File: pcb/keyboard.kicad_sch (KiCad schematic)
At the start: 22 parts, among them J1 Conn_ARM_JTAG_SWD_10, SW1 SW_PUSH, U1 nRF52840-QFXX, X1 32MHz

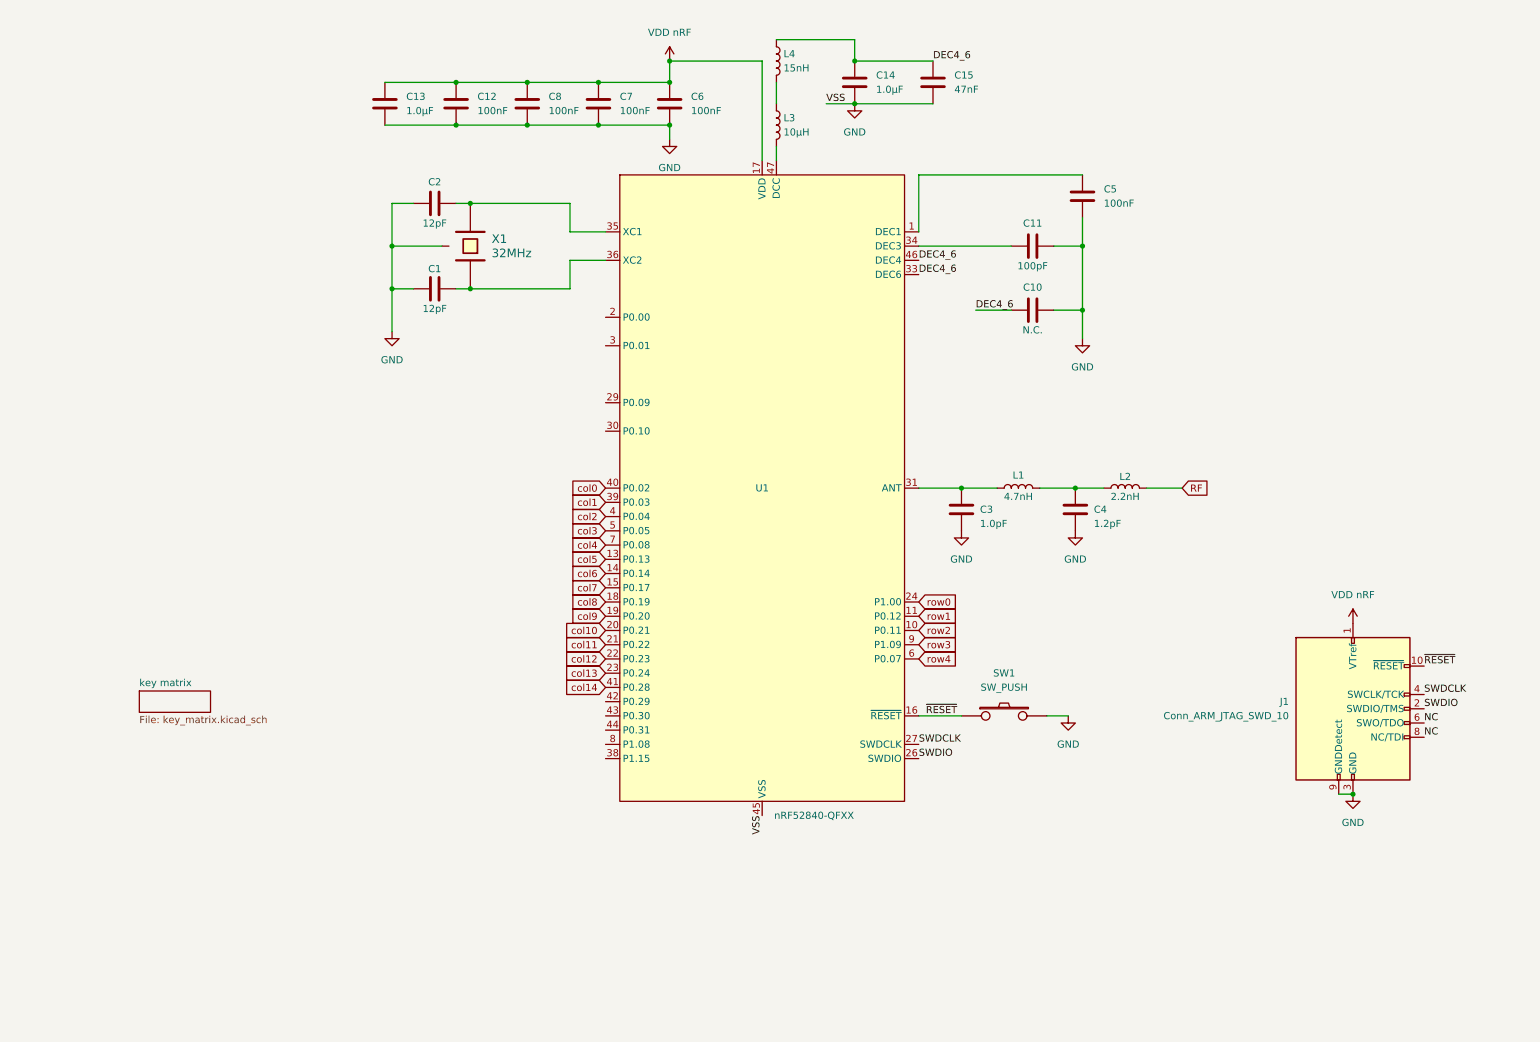
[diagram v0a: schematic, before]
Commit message: Change uc footprint over to aQFN to access USB pins
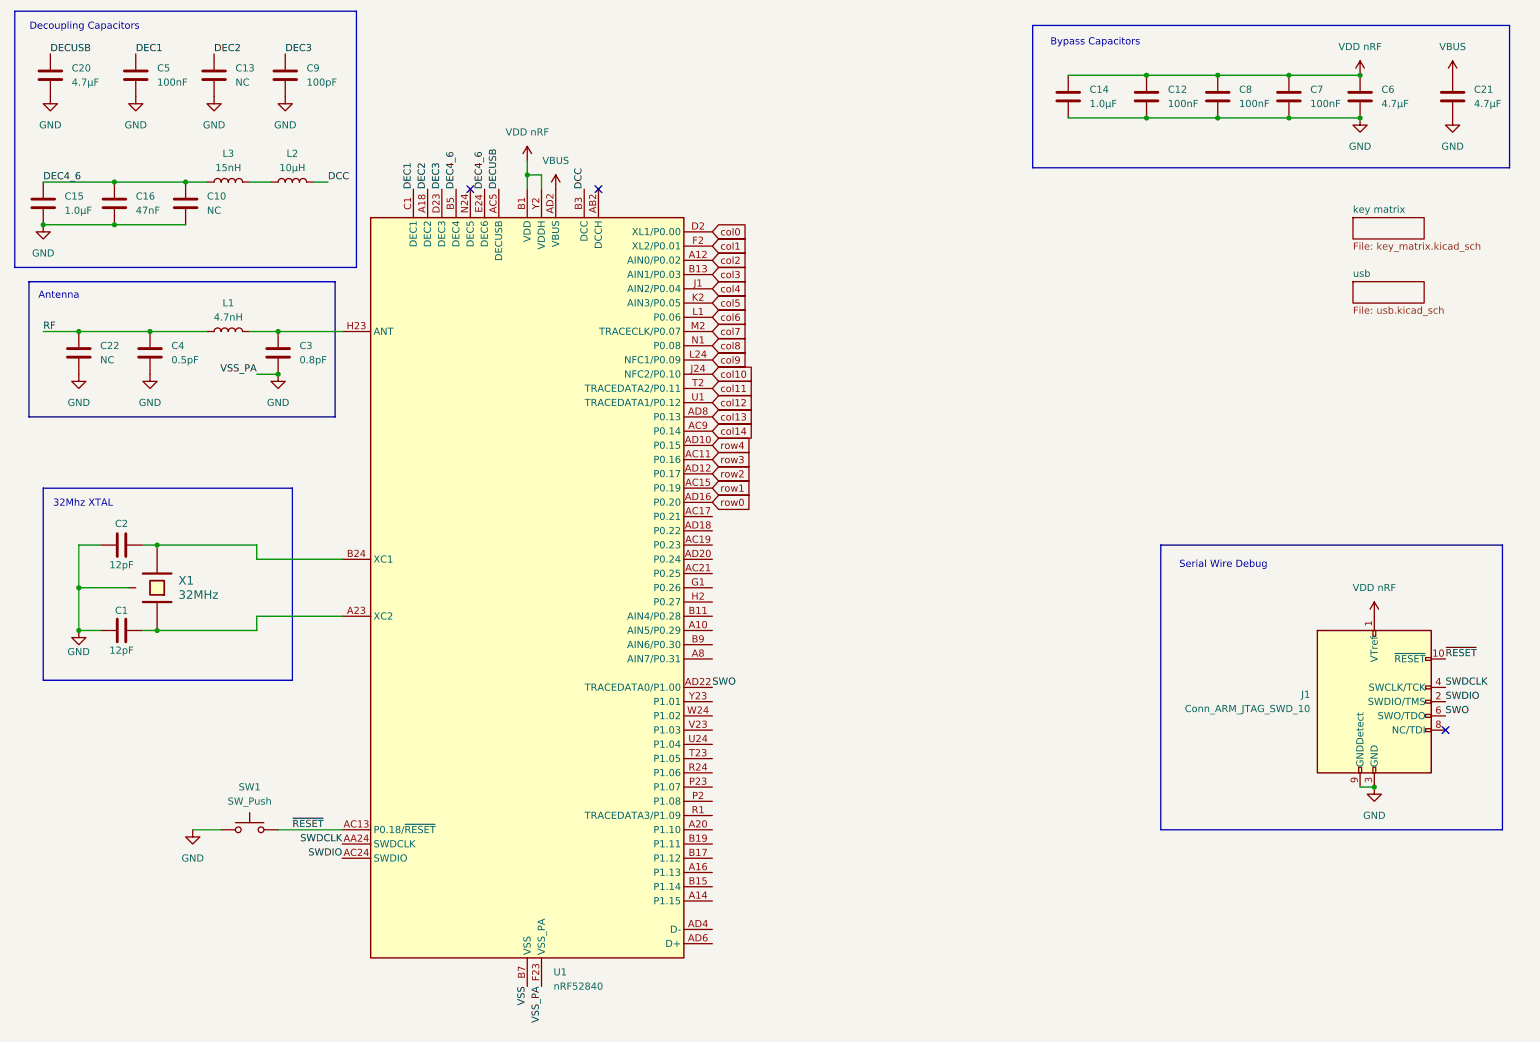
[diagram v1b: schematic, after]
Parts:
- removed C11: 100pF, symbol Device:C
- removed L4: 15nH, symbol Device:L
- removed SW1: SW_PUSH, symbol keyboard_parts:SW_PUSH
- removed U1: nRF52840-QFXX, Package_DFN_QFN:QFN-48-1EP_6x6mm_P0.4mm_EP4.6x4.6mm_ThermalVias, symbol nordic-lib-kicad-nrf52:nRF52840-QFXX
- added C16: 47nF, symbol Device:C
- added C20, C21: 4.7µF, symbol Device:C
- added C22: NC, symbol Device:C
- added C9: 100pF, symbol Device:C
- added SW1: SW_Push, symbol Switch:SW_Push
- added U1: nRF52840, Package_DFN_QFN:Nordic_AQFN-73-1EP_7x7mm_P0.5mm, symbol MCU_Nordic:nRF52840
- C10: value N.C. -> NC
- C13: value 1.0μF -> NC
- C14: value 1.0μF -> 1.0µF
- C15: value 47nF -> 1.0µF
- C3: value 1.0pF -> 0.8pF
- C4: value 1.2pF -> 0.5pF
- C6: value 100nF -> 4.7µF
- L2: value 2.2nH -> 10µH
- L3: value 10μH -> 15nH
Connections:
- net DEC4_6: now also L3.1, C16.1, U1.B5 (DEC4), U1.E24 (DEC6); no longer C14.1
- net GND: now also C16.2, C20.2, C21.2, C22.2, C9.2, SW1.1, U1.F23 (VSS_PA)
- net RF: now also C4.1, L1.1, C22.1; no longer L2.2
- net SWDCLK: now also U1.AA24 (SWDCLK)
- net SWDIO: now also U1.AC24 (SWDIO)
- net VDD nRF: now also C14.1, U1.A22 (VDD), U1.AD14 (VDD), U1.AD23 (VDD), U1.B1 (VDD), U1.W1 (VDD), U1.Y2 (VDDH); no longer C13.1
- net col0: now also U1.D2 (XL1/P0.00)
- net col1: now also U1.F2 (XL2/P0.01)
- net col10: now also U1.J24 (NFC2/P0.10)
- net col11: now also U1.T2 (TRACEDATA2/P0.11)
- net col12: now also U1.U1 (TRACEDATA1/P0.12)
- net col13: now also U1.AD8 (P0.13)
- net col14: now also U1.AC9 (P0.14)
- net col2: now also U1.A12 (AIN0/P0.02)
- net col3: now also U1.B13 (AIN1/P0.03)
- net col4: now also U1.J1 (AIN2/P0.04)
- net col5: now also U1.K2 (AIN3/P0.05)
- net col6: now also U1.L1 (P0.06)
- net col7: now also U1.M2 (TRACECLK/P0.07)
- net col8: now also U1.N1 (P0.08)
- net col9: now also U1.L24 (NFC1/P0.09)
- net row0: now also U1.AD16 (P0.20)
- net row1: now also U1.AC15 (P0.19)
- net row2: now also U1.AD12 (P0.17)
- net row3: now also U1.AC11 (P0.16)
- net row4: now also U1.AD10 (P0.15)
- net ~{RESET}: now also SW1.2, U1.AC13 (P0.18/~{RESET})
- net at L3.2: now also L2.1
- net DEC1: now reaches C5.1
- net DEC1: now also U1.C1 (DEC1)
- net at C3.1: now also L1.2, U1.H23 (ANT); no longer L1.1
- net at C2.2, X1.2: now also U1.B24 (XC1)
- net at C1.2, X1.1: now also U1.A23 (XC2)
- net NC: no longer names the net of J1.8 (NC/TDI)
- net NC: no longer J1.6 (SWO/TDO)
- new net DCC: L2.2, U1.B3 (DCC)
- new net DEC2: C13.1, U1.A18 (DEC2)
- new net DEC3: C9.1, U1.D23 (DEC3)
- new net DECUSB: C20.1, U1.AC5 (DECUSB)
- new net SWO: J1.6 (SWO/TDO), U1.AD22 (TRACEDATA0/P1.00)
- new net VBUS: C21.1, U1.AD2 (VBUS)
- new net VSS: U1.B7 (VSS), U1.EP (VSS)
- no-connect marks 0 -> 3
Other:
- added sheet usb (usb.kicad_sch)
- note added: "32Mhz XTAL"
- note added: "Antenna"
- note added: "Bypass Capacitors"
- note added: "Decoupling Capacitors"
- note added: "Serial Wire Debug"
- moved on the sheet: J1

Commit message: WIP: power / battery schematic
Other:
- sheet usb renamed charging
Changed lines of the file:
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@@
 			(color 0 0 0 0.0000)
 		)
-		(property "Sheetname" "usb"
+		(property "Sheetname" "charging"
 			(at 252.73 61.5184 0)
 			(effects

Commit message: WIP: power / battery schematic 2
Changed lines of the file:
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@@
 	)
 	(sheet
-		(at 252.73 62.23)
-		(size 12.7 3.81)
+		(at 251.46 63.5)
+		(size 22.86 7.62)
 		(exclude_from_sim no)
 		(in_bom yes)
@@
 		)
 		(property "Sheetname" "charging"
-			(at 252.73 61.5184 0)
+			(at 251.46 62.7884 0)
 			(effects
 				(font
@@
 		)
 		(property "Sheetfile" "usb.kicad_sch"
-			(at 252.73 66.6246 0)
+			(at 251.46 71.7046 0)
 			(effects
 				(font

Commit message: First version of power circuitry complete?
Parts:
- added C19: 4.7µF, symbol Device:C
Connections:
- net GND: now also C19.2
- net VDD nRF: no longer U1.Y2 (VDDH)
- net USB_D-: now reaches U1.AD4 (D-)
- net USB_D+: now reaches U1.AD6 (D+)
- new net VDDH: C19.1, U1.Y2 (VDDH)
- no-connect marks 3 -> 29
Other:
- sheet charging renamed power
- moved on the sheet: C12, C14, C6, C7, C8

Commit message: Start assigning footprints
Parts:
- C1, C10, C12, C13, C14, C15, C16, C19, C2, C20, C21, C22, C3, C4, C5, C6, C7, C8, C9: footprint (none) -> Capacitor_SMD:C_0805_2012Metric_Pad1.18x1.45mm_HandSolder
- L1, L2, L3: footprint (none) -> Inductor_SMD:L_0805_2012Metric_Pad1.05x1.20mm_HandSolder
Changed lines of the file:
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@@
 			)
 		)
-		(property "Footprint" ""
+		(property "Footprint" "Capacitor_SMD:C_0805_2012Metric_Pad1.18x1.45mm_HandSolder"
 			(at 20.0152 52.07 0)
 			(effects
@@
 			)
 		)
-		(property "Footprint" ""
+		(property "Footprint" "Capacitor_SMD:C_0805_2012Metric_Pad1.18x1.45mm_HandSolder"
 			(at 21.2852 29.21 0)
 			(effects
@@
 			)
 		)
-		(property "Footprint" ""
+		(property "Footprint" "Capacitor_SMD:C_0805_2012Metric_Pad1.18x1.45mm_HandSolder"
 			(at 215.5952 33.02 0)
 			(effects
@@
 			)
 		)
-		(property "Footprint" ""
+		(property "Footprint" "Capacitor_SMD:C_0805_2012Metric_Pad1.18x1.45mm_HandSolder"
 			(at 188.9252 33.02 0)
 			(effects
@@
 			)
 		)
-		(property "Footprint" ""
+		(property "Footprint" "Capacitor_SMD:C_0805_2012Metric_Pad1.18x1.45mm_HandSolder"
 			(at 32.7152 52.07 0)
 			(effects
@@
 			)
 		)
-		(property "Footprint" ""
+		(property "Footprint" "Capacitor_SMD:C_0805_2012Metric_Pad1.18x1.45mm_HandSolder"
 			(at 26.3652 78.74 0)
 			(effects
@@
 			)
 		)
-		(property "Footprint" ""
+		(property "Footprint" "Capacitor_SMD:C_0805_2012Metric_Pad1.18x1.45mm_HandSolder"
 			(at 202.8952 33.02 0)
 			(effects
@@
 			)
 		)
-		(property "Footprint" ""
+		(property "Footprint" "Capacitor_SMD:C_0805_2012Metric_Pad1.18x1.45mm_HandSolder"
 			(at 50.4952 29.21 0)
 			(effects
@@
 			)
 		)
-		(property "Footprint" ""
+		(property "Footprint" "Capacitor_SMD:C_0805_2012Metric_Pad1.18x1.45mm_HandSolder"
 			(at 228.2952 33.02 0)
 			(effects
@@
 			)
 		)
-		(property "Footprint" ""
+		(property "Footprint" "Inductor_SMD:L_0805_2012Metric_Pad1.05x1.20mm_HandSolder"
 			(at 63.5 44.45 0)
 			(effects
@@
 			)
 		)
-		(property "Footprint" ""
+		(property "Footprint" "Inductor_SMD:L_0805_2012Metric_Pad1.05x1.20mm_HandSolder"
 			(at 52.07 71.12 0)
 			(effects
@@
 			)
 		)
-		(property "Footprint" ""
+		(property "Footprint" "Capacitor_SMD:C_0805_2012Metric_Pad1.18x1.45mm_HandSolder"
 			(at 36.83 123.4948 0)
 			(effects
@@
 			)
 		)
-		(property "Footprint" ""
+		(property "Footprint" "Capacitor_SMD:C_0805_2012Metric_Pad1.18x1.45mm_HandSolder"
 			(at 45.4152 52.07 0)
 			(effects
@@
 			)
 		)
-		(property "Footprint" ""
+		(property "Footprint" "Capacitor_SMD:C_0805_2012Metric_Pad1.18x1.45mm_HandSolder"
 			(at 271.4752 33.02 0)
 			(effects
@@
 			)
 		)
-		(property "Footprint" ""
+		(property "Footprint" "Capacitor_SMD:C_0805_2012Metric_Pad1.18x1.45mm_HandSolder"
 			(at 61.9252 78.74 0)
 			(effects
@@
 			)
 		)
-		(property "Footprint" ""
+		(property "Footprint" "Inductor_SMD:L_0805_2012Metric_Pad1.05x1.20mm_HandSolder"
 			(at 52.07 44.45 0)
 			(effects
@@
 			)
 		)
-		(property "Footprint" ""
+		(property "Footprint" "Capacitor_SMD:C_0805_2012Metric_Pad1.18x1.45mm_HandSolder"
 			(at 36.5252 29.21 0)
 			(effects
@@
 			)
 		)
-		(property "Footprint" ""
+		(property "Footprint" "Capacitor_SMD:C_0805_2012Metric_Pad1.18x1.45mm_HandSolder"
 			(at 39.0652 78.74 0)
 			(effects
@@
 			)
 		)
-		(property "Footprint" ""
+		(property "Footprint" "Capacitor_SMD:C_0805_2012Metric_Pad1.18x1.45mm_HandSolder"
 			(at 63.1952 29.21 0)
 			(effects
@@
 			)
 		)
-		(property "Footprint" ""
+		(property "Footprint" "Capacitor_SMD:C_0805_2012Metric_Pad1.18x1.45mm_HandSolder"
 			(at 36.83 108.2548 0)
 			(effects
@@
 					(size 1.524 1.524)
 				)
+				(hide yes)
 			)
 		)
@@
 			)
 		)
-		(property "Footprint" ""
+		(property "Footprint" "Capacitor_SMD:C_0805_2012Metric_Pad1.18x1.45mm_HandSolder"
 			(at 256.2352 33.02 0)
 			(effects
@@
 			)
 		)
-		(property "Footprint" ""
+		(property "Footprint" "Capacitor_SMD:C_0805_2012Metric_Pad1.18x1.45mm_HandSolder"
 			(at 240.9952 33.02 0)
 			(effects

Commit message: Finish power circuitry
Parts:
- added R10: 10k, symbol Device:R
- C10, C13, C22: now not fitted
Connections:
- net VDDH: now also R10.1
- net ~{RESET}: now also R10.2
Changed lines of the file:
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@@
 	)
 	(junction
+		(at 62.23 160.02)
+		(diameter 0)
+		(color 0 0 0 0)
+	)
+	(junction
 		(at 201.93 25.4)
 		(diameter 0)
@@
 	(wire
 		(pts
-			(xy 60.96 160.02) (xy 72.39 160.02)
+			(xy 62.23 144.78) (xy 62.23 147.32)
+		)
+		(stroke
+			(width 0)
+			(type default)
+		)
+	)
+	(wire
+		(pts
+			(xy 60.96 160.02) (xy 62.23 160.02)
 		)
 		(stroke
@@
 	(wire
 		(pts
+			(xy 62.23 160.02) (xy 72.39 160.02)
+		)
+		(stroke
+			(width 0)
+			(type default)
+		)
+	)
+	(wire
+		(pts
 			(xy 25.4 116.84) (xy 25.4 109.22)
 		)
@@
 	(wire
 		(pts
+			(xy 62.23 154.94) (xy 62.23 160.02)
+		)
+		(stroke
+			(width 0)
+			(type default)
+		)
+	)
+	(wire
+		(pts
 			(xy 55.88 71.12) (xy 60.96 71.12)
 		)
@@
 		(in_bom yes)
 		(on_board yes)
-		(dnp no)
+		(dnp yes)
 		(fields_autoplaced yes)
 		(property "Reference" "C22"
@@
 		(in_bom yes)
 		(on_board yes)
-		(dnp no)
+		(dnp yes)
 		(fields_autoplaced yes)
 		(property "Reference" "C13"
@@
 	)
 	(symbol
+		(lib_id "Device:R")
+		(at 62.23 151.13 0)
+		(unit 1)
+		(exclude_from_sim no)
+		(in_bom yes)
+		(on_board yes)
+		(dnp yes)
+		(fields_autoplaced yes)
+		(property "Reference" "R10"
+			(at 64.77 149.8599 0)
+			(effects
+				(font
+					(size 1.27 1.27)
+				)
+				(justify left)
+			)
+		)
+		(property "Value" "10k"
+			(at 64.77 152.3999 0)
+			(effects
+				(font
+					(size 1.27 1.27)
+				)
+				(justify left)
+			)
+		)
+		(property "Footprint" ""
+			(at 60.452 151.13 90)
+			(effects
+				(font
+					(size 1.27 1.27)
+				)
+				(hide yes)
+			)
+		)
+		(property "Datasheet" "~"
+			(at 62.23 151.13 0)
+			(effects
+				(font
+					(size 1.27 1.27)
+				)
+				(hide yes)
+			)
+		)
+		(property "Description" "Resistor"
+			(at 62.23 151.13 0)
+			(effects
+				(font
+					(size 1.27 1.27)
+				)
+				(hide yes)
+			)
+		)
+		(pin "1"
+		)
+		(pin "2"
+		)
+		(instances
+			(project ""
+				(path "/39e5e398-89ad-4475-a3bf-05d3324a2c58"
+					(reference "R10")
+					(unit 1)
+				)
+			)
+		)
+	)
+	(symbol
 		(lib_id "power:VBUS")
 		(at 111.76 43.18 0)
@@
 		(in_bom yes)
 		(on_board yes)
-		(dnp no)
+		(dnp yes)
 		(fields_autoplaced yes)
 		(property "Reference" "C10"
@@
 					(unit 1)
 				)
+			)
+		)
+	)
+	(symbol
+		(lib_id "power:VDD")
+		(at 62.23 144.78 0)
+		(unit 1)
+		(exclude_from_sim no)
+		(in_bom yes)
+		(on_board yes)
+		(dnp no)
+		(fields_autoplaced yes)
+		(property "Reference" "#PWR033"
+			(at 62.23 148.59 0)
+			(effects
+				(font
+					(size 1.27 1.27)
+				)
+				(hide yes)
+			)
+		)
+		(property "Value" "VDDH"
+			(at 62.23 139.7 0)
+			(effects
+				(font
+					(size 1.27 1.27)
+				)
+			)
+		)
+		(property "Footprint" ""
+			(at 62.23 144.78 0)
+			(effects
+				(font
+					(size 1.27 1.27)
+				)
+				(hide yes)
+			)
+		)
+		(property "Datasheet" ""
+			(at 62.23 144.78 0)
+			(effects
+				(font
+					(size 1.27 1.27)
+				)
+				(hide yes)
+			)
+		)
+		(property "Description" "Power symbol creates a global label with name \"VDD\""
+			(at 62.23 144.78 0)
+			(effects
+				(font
+					(size 1.27 1.27)
+				)
+				(hide yes)
+			)
+		)
+		(pin "1"
+		)
+		(instances
+			(project "keyboard"
+				(path "/39e5e398-89ad-4475-a3bf-05d3324a2c58"
+					(reference "#PWR033")
+					(unit 1)
+				)

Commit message: Fill in some more components
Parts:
- R10: footprint (none) -> Resistor_SMD:R_0805_2012Metric_Pad1.20x1.40mm_HandSolder
- X1: footprint (none) -> Crystal:Crystal_SMD_2016-4Pin_2.0x1.6mm
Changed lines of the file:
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@@
 		)
 		(instances
-			(project ""
+			(project "keyboard"
 				(path "/39e5e398-89ad-4475-a3bf-05d3324a2c58"
 					(reference "#PWR01")
@@
 		)
 		(instances
-			(project ""
+			(project "keyboard"
 				(path "/39e5e398-89ad-4475-a3bf-05d3324a2c58"
 					(reference "C20")
@@
 		)
 		(instances
-			(project ""
+			(project "keyboard"
 				(path "/39e5e398-89ad-4475-a3bf-05d3324a2c58"
 					(reference "SW1")
@@
 		)
 		(instances
-			(project ""
+			(project "keyboard"
 				(path "/39e5e398-89ad-4475-a3bf-05d3324a2c58"
 					(reference "J1")
@@
 		)
 		(instances
-			(project ""
+			(project "keyboard"
 				(path "/39e5e398-89ad-4475-a3bf-05d3324a2c58"
 					(reference "#PWR07")
@@
 		)
 		(instances
-			(project ""
+			(project "keyboard"
 				(path "/39e5e398-89ad-4475-a3bf-05d3324a2c58"
 					(reference "#PWR04")
@@
 		)
 		(instances
-			(project ""
+			(project "keyboard"
 				(path "/39e5e398-89ad-4475-a3bf-05d3324a2c58"
 					(reference "U1")
@@
 			)
 		)
-		(property "Footprint" ""
+		(property "Footprint" "Resistor_SMD:R_0805_2012Metric_Pad1.20x1.40mm_HandSolder"
 			(at 60.452 151.13 90)
 			(effects
@@
 		)
 		(instances
-			(project ""
+			(project "keyboard"
 				(path "/39e5e398-89ad-4475-a3bf-05d3324a2c58"
 					(reference "R10")
@@
 		)
 		(instances
-			(project ""
+			(project "keyboard"
 				(path "/39e5e398-89ad-4475-a3bf-05d3324a2c58"
 					(reference "#PWR08")
@@
 		)
 		(instances
-			(project ""
+			(project "keyboard"
 				(path "/39e5e398-89ad-4475-a3bf-05d3324a2c58"
 					(reference "L1")
@@
 		)
 		(instances
-			(project ""
+			(project "keyboard"
 				(path "/39e5e398-89ad-4475-a3bf-05d3324a2c58"
 					(reference "#PWR09")
@@
 		)
 		(instances
-			(project ""
+			(project "keyboard"
 				(path "/39e5e398-89ad-4475-a3bf-05d3324a2c58"
 					(reference "#PWR02")
@@
 		)
 		(instances
-			(project ""
+			(project "keyboard"
 				(path "/39e5e398-89ad-4475-a3bf-05d3324a2c58"
 					(reference "C3")
@@
 		)
 		(instances
-			(project ""
+			(project "keyboard"
 				(path "/39e5e398-89ad-4475-a3bf-05d3324a2c58"
 					(reference "#PWR014")
@@
 			)
 		)
-		(property "Footprint" ""
+		(property "Footprint" "Crystal:Crystal_SMD_2016-4Pin_2.0x1.6mm"
 			(at 39.37 116.84 0)
 			(effects
@@
 		)
 		(instances
-			(project ""
+			(project "keyboard"
 				(path "/39e5e398-89ad-4475-a3bf-05d3324a2c58"
 					(reference "C6")
